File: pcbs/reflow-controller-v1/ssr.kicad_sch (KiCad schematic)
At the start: 7 parts, among them U301 MOC3043SM

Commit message: footprint assignement fixed; buzzer added
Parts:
- C301: footprint Capacitor_SMD:C_2220_5650Metric -> Capacitor_SMD:C_2220_5750Metric
- U301: footprint (none) -> Package_DIP:DIP-6_W7.62mm_SMDSocket_SmallPads
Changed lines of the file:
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@@
 			)
 		)
-		(property "Footprint" ""
+		(property "Footprint" "Package_DIP:DIP-6_W7.62mm_SMDSocket_SmallPads"
 			(at 134.62 95.25 0)
 			(effects
@@
 			)
 		)
-		(property "Footprint" "Capacitor_SMD:C_2220_5650Metric"
+		(property "Footprint" "Capacitor_SMD:C_2220_5750Metric"
 			(at 197.8152 107.95 0)
 			(effects

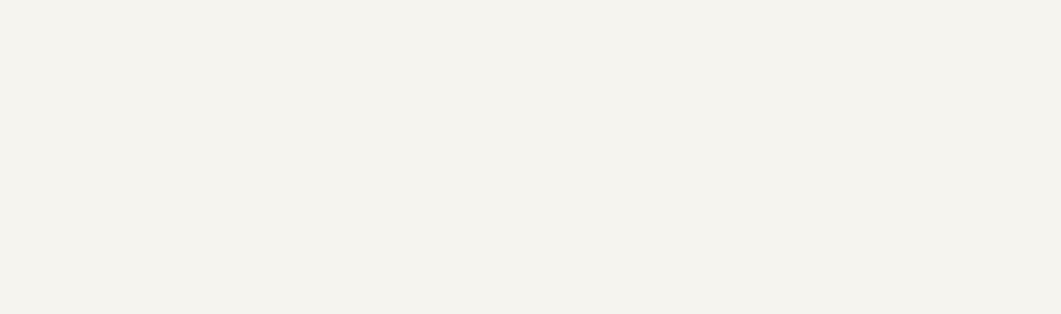
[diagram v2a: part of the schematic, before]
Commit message: SSR schematic: add link to datasheet/reference schematic
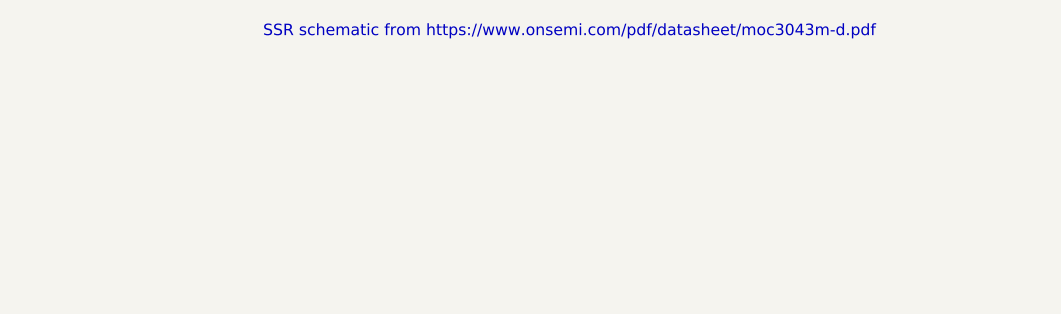
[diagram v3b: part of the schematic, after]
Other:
- note added: "SSR schematic from https://www.onsemi.com/pdf/datasheet/moc3043m-d.pdf"
